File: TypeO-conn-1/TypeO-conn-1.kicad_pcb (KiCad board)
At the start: 2 copper layers, 5 parts, among them J1 USB_C_Receptacle_USB2.0, J2 , SW1 SW_DIP_x01

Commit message: Update PCB
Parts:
- moved J2 2.54 mm to (124.5, 76.2)
- moved SW1 2.54 mm to (119.4, 86.4)
- moved R2 1.79 mm to (112.5, 76.2)
- moved R1 1.46 mm to (114.3, 83.6)
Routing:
- net Net-(J1-PadA6): track 23.7 -> 16.0 mm, vias 0 -> 1
- net Net-(J1-PadA1): track 31.5 -> 24.7 mm
- net Net-(J1-PadA4): track 19.3 -> 16.9 mm
- net Net-(SW1-Pad2): track 7.88 -> 5.64 mm
- net Net-(J1-PadA5): track 13.6 -> 11.8 mm
- net Net-(J1-PadA7): track 18.6 -> 16.8 mm
- net Net-(J1-PadB5): track 14.1 -> 13.3 mm
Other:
- board outline added: 24 x 19.6 mm
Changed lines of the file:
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@@
     (property "Sheetname" "")
     (attr smd)
-    (fp_text reference "J1" (at -6.670499 0.12134 180) (layer "F.SilkS")
+    (fp_text reference "J1" (at -6.404035 -0.274964 180) (layer "F.SilkS")
       (effects (font (size 1 1) (thickness 0.15)))
     )
@@
   )
   (footprint "Resistor_THT:R_Axial_DIN0207_L6.3mm_D2.5mm_P7.62mm_Horizontal" (layer "F.Cu")
-    (at 114.3 76.2)
+    (at 112.505976 76.246718)
     (descr "Resistor, Axial_DIN0207 series, Axial, Horizontal, pin pitch=7.62mm, 0.25W = 1/4W, length*diameter=6.3*2.5mm^2, http://cdn-reichelt.de/documents/datenblatt/B400/1_4W%23YAG.pdf")
     (tags "Resistor Axial_DIN0207 series Axial Horizontal pin pitch 7.62mm 0.25W = 1/4W length 6.3mm diameter 2.5mm")
@@
     (property "Sheetname" "")
     (attr through_hole)
-    (fp_text reference "R2" (at 1.522976 -2.602604) (layer "F.SilkS")
-      (effects (font (size 1 1) (thickness 0.15)))
-    )
-    (fp_text value "10K" (at 5.08 -2.54) (layer "F.Fab")
+    (fp_text reference "R2" (at 1.848743 2.473275) (layer "F.SilkS")
+      (effects (font (size 1 1) (thickness 0.15)))
+    )
+    (fp_text value "10K" (at 5.54862 2.617426) (layer "F.Fab")
       (effects (font (size 1 1) (thickness 0.15)))
     )
@@
   )
   (footprint "Connector_PinHeader_2.54mm:PinHeader_1x05_P2.54mm_Vertical" (layer "F.Cu")
-    (at 127 76.2)
+    (at 124.46 76.2)
     (descr "Through hole straight pin header, 1x05, 2.54mm pitch, single row")
     (tags "Through hole pin header THT 1x05 2.54mm single row")
@@
     (property "Sheetname" "")
     (attr through_hole)
-    (fp_text reference "J2" (at 0 -2.33) (layer "F.SilkS")
+    (fp_text reference "J2" (at -2.561376 2.231691) (layer "F.SilkS")
       (effects (font (size 1 1) (thickness 0.15)))
     )
@@
   )
   (footprint "Resistor_THT:R_Axial_DIN0207_L6.3mm_D2.5mm_P7.62mm_Horizontal" (layer "F.Cu")
-    (at 114.3 85.09 -90)
+    (at 114.327258 83.628569 -90)
     (descr "Resistor, Axial_DIN0207 series, Axial, Horizontal, pin pitch=7.62mm, 0.25W = 1/4W, length*diameter=6.3*2.5mm^2, http://cdn-reichelt.de/documents/datenblatt/B400/1_4W%23YAG.pdf")
     (tags "Resistor Axial_DIN0207 series Axial Horizontal pin pitch 7.62mm 0.25W = 1/4W length 6.3mm diameter 2.5mm")
@@
     (property "Sheetname" "")
     (attr through_hole)
-    (fp_text reference "R1" (at 1.4988 2.373258 180) (layer "F.SilkS")
-      (effects (font (size 1 1) (thickness 0.15)))
-    )
-    (fp_text value "10K" (at 4.719649 2.429764 90) (layer "F.Fab")
+    (fp_text reference "R1" (at 5.470301 2.951661 180) (layer "F.SilkS")
+      (effects (font (size 1 1) (thickness 0.15)))
+    )
+    (fp_text value "10K" (at 1.482121 2.375057 90) (layer "F.Fab")
       (effects (font (size 1 1) (thickness 0.15)))
     )
@@
   )
   (footprint "Button_Switch_SMD:SW_DIP_SPSTx01_Slide_Omron_A6S-110x_W8.9mm_P2.54mm" (layer "F.Cu")
-    (at 119.38 88.9 90)
+    (at 119.38 86.36 90)
     (descr "SMD 1x-dip-switch SPST Omron_A6S-110x, Slide, row spacing 8.9 mm (350 mils), body size  (see http://omronfs.omron.com/en_US/ecb/products/pdf/en-a6s.pdf)")
     (tags "SMD DIP Switch SPST Slide 8.9mm 350mil")
@@
     (property "Sheetname" "")
     (attr smd)
-    (fp_text reference "SW1" (at 1.802645 3.847967 180) (layer "F.SilkS")
+    (fp_text reference "SW1" (at -2.883021 3.75 180) (layer "F.SilkS")
       (effects (font (size 1 1) (thickness 0.15)))
     )
@@
     )
   )
-  (segment (start 114.3 88.9) (end 114.3 85.09) (width 0.25) (layer "F.Cu") (net 1))
-  (segment (start 127 86.36) (end 120.01 93.35) (width 0.25) (layer "F.Cu") (net 1))
-  (segment (start 113.59 84.38) (end 109.73 84.38) (width 0.25) (layer "F.Cu") (net 1))
-  (segment (start 114.3 85.09) (end 113.59 84.38) (width 0.25) (layer "F.Cu") (net 1))
-  (segment (start 114.3 76.2) (end 112.32 78.18) (width 0.25) (layer "F.Cu") (net 1))
-  (segment (start 118.75 93.35) (end 114.3 88.9) (width 0.25) (layer "F.Cu") (net 1))
-  (segment (start 112.32 78.18) (end 109.73 78.18) (width 0.25) (layer "F.Cu") (net 1))
-  (segment (start 119.38 93.35) (end 118.75 93.35) (width 0.25) (layer "F.Cu") (net 1))
-  (segment (start 120.01 93.35) (end 119.38 93.35) (width 0.25) (layer "F.Cu") (net 1))
-  (segment (start 121.454211 75.075489) (end 117.5997 78.93) (width 0.25) (layer "F.Cu") (net 2))
-  (segment (start 117.5997 78.93) (end 109.73 78.93) (width 0.25) (layer "F.Cu") (net 2))
-  (segment (start 127 76.2) (end 125.875489 75.075489) (width 0.25) (layer "F.Cu") (net 2))
-  (segment (start 125.875489 75.075489) (end 121.454211 75.075489) (width 0.25) (layer "F.Cu") (net 2))
-  (segment (start 121.92 76.2) (end 118.59 79.53) (width 0.25) (layer "F.Cu") (net 3))
-  (segment (start 118.59 79.53) (end 109.73 79.53) (width 0.25) (layer "F.Cu") (net 3))
+  (gr_line (start 127 73.66) (end 127 88.9) (layer "Edge.Cuts") (width 0.1))
+  (gr_line (start 127 88.9) (end 121.32202 93.135099) (layer "Edge.Cuts") (width 0.1))
+  (gr_line (start 112.288553 93.087049) (end 107.195216 88.089812) (layer "Edge.Cuts") (width 0.1))
+  (gr_line (start 103.062885 88.089812) (end 103.014836 73.578605) (layer "Edge.Cuts") (width 0.1))
+  (gr_line (start 107.195216 88.089812) (end 103.062885 88.089812) (layer "Edge.Cuts") (width 0.1))
+  (gr_line (start 121.32202 93.135099) (end 112.288553 93.087049) (layer "Edge.Cuts") (width 0.1))
+  (gr_line (start 103.014836 73.578605) (end 106.68 73.578605) (layer "Edge.Cuts") (width 0.1))
+  (gr_line (start 106.68 73.578605) (end 127 73.66) (layer "Edge.Cuts") (width 0.1))
+  (segment (start 114.327258 85.757258) (end 119.38 90.81) (width 0.5) (layer "F.Cu") (net 1))
+  (segment (start 113.575827 84.38) (end 114.327258 83.628569) (width 0.5) (layer "F.Cu") (net 1))
+  (segment (start 120.01 90.81) (end 124.46 86.36) (width 0.5) (layer "F.Cu") (net 1))
+  (segment (start 119.38 90.81) (end 120.01 90.81) (width 0.5) (layer "F.Cu") (net 1))
+  (segment (start 110.572694 78.18) (end 109.73 78.18) (width 0.5) (layer "F.Cu") (net 1))
+  (segment (start 114.327258 83.628569) (end 114.327258 85.757258) (width 0.5) (layer "F.Cu") (net 1))
+  (segment (start 109.73 84.38) (end 113.575827 84.38) (width 0.5) (layer "F.Cu") (net 1))
+  (segment (start 112.505976 76.246718) (end 110.572694 78.18) (width 0.5) (layer "F.Cu") (net 1))
+  (segment (start 116.918282 74.997207) (end 112.985489 78.93) (width 0.5) (layer "F.Cu") (net 2))
+  (segment (start 112.985489 78.93) (end 109.73 78.93) (width 0.5) (layer "F.Cu") (net 2))
+  (segment (start 123.257207 74.997207) (end 116.84 74.997207) (width 0.5) (layer "F.Cu") (net 2))
+  (segment (start 124.46 76.2) (end 123.257207 74.997207) (width 0.5) (layer "F.Cu") (net 2))
+  (segment (start 116.842694 79.53) (end 109.73 79.53) (width 0.25) (layer "F.Cu") (net 3))
+  (segment (start 120.125976 76.246718) (end 116.842694 79.53) (width 0.25) (layer "F.Cu") (net 3))
+  (segment (start 114.327258 91.248569) (end 113.12539 91.248569) (width 0.25) (layer "F.Cu") (net 5))
   (segment (start 107.88048 83.595498) (end 108.945978 82.53) (width 0.25) (layer "F.Cu") (net 5))
-  (segment (start 107.88048 86.29048) (end 107.88048 83.595498) (width 0.25) (layer "F.Cu") (net 5))
   (segment (start 108.945978 82.53) (end 109.73 82.53) (width 0.25) (layer "F.Cu") (net 5))
-  (segment (start 114.3 92.71) (end 107.88048 86.29048) (width 0.25) (layer "F.Cu") (net 5))
-  (segment (start 121.190229 77.565489) (end 127.486499 77.565489) (width 0.25) (layer "F.Cu") (net 10))
-  (segment (start 109.73 81.03) (end 117.725718 81.03) (width 0.25) (layer "F.Cu") (net 10))
-  (segment (start 128.174511 80.105489) (end 127 81.28) (width 0.25) (layer "F.Cu") (net 10))
-  (segment (start 117.725718 81.03) (end 121.190229 77.565489) (width 0.25) (layer "F.Cu") (net 10))
-  (segment (start 128.174511 78.253501) (end 128.174511 80.105489) (width 0.25) (layer "F.Cu") (net 10))
-  (segment (start 127.486499 77.565489) (end 128.174511 78.253501) (width 0.25) (layer "F.Cu") (net 10))
-  (segment (start 109.73 82.03) (end 123.71 82.03) (width 0.25) (layer "F.Cu") (net 11))
-  (segment (start 123.71 82.03) (end 127 78.74) (width 0.25) (layer "F.Cu") (net 11))
-  (segment (start 126.37 84.45) (end 127 83.82) (width 0.25) (layer "F.Cu") (net 12))
-  (segment (start 119.38 84.45) (end 126.37 84.45) (width 0.25) (layer "F.Cu") (net 12))
+  (segment (start 113.12539 91.248569) (end 107.88048 86.003659) (width 0.25) (layer "F.Cu") (net 5))
+  (segment (start 107.88048 86.003659) (end 107.88048 83.595498) (width 0.25) (layer "F.Cu") (net 5))
+  (segment (start 117.931641 79.597769) (end 120.273755 79.597769) (width 0.25) (layer "F.Cu") (net 10))
+  (segment (start 109.73 81.03) (end 116.49941 81.03) (width 0.25) (layer "F.Cu") (net 10))
+  (segment (start 116.49941 81.03) (end 117.931641 79.597769) (width 0.25) (layer "F.Cu") (net 10))
+  (via (at 120.273755 79.597769) (size 0.8) (drill 0.4) (layers "F.Cu" "B.Cu") (net 10))
+  (segment (start 121.955986 81.28) (end 120.273755 79.597769) (width 0.25) (layer "B.Cu") (net 10))
+  (segment (start 124.46 81.28) (end 121.955986 81.28) (width 0.25) (layer "B.Cu") (net 10))
+  (segment (start 123.71 78.74) (end 124.46 78.74) (width 0.25) (layer "F.Cu") (net 11))
+  (segment (start 118.269603 80.486115) (end 122.713885 80.486115) (width 0.25) (layer "F.Cu") (net 11))
+  (segment (start 116.725718 82.03) (end 118.269603 80.486115) (width 0.25) (layer "F.Cu") (net 11))
+  (segment (start 109.73 82.03) (end 116.725718 82.03) (width 0.25) (layer "F.Cu") (net 11))
+  (segment (start 122.713885 80.486115) (end 124.46 78.74) (width 0.25) (layer "F.Cu") (net 11))
+  (segment (start 119.38 82.47952) (end 119.94952 82.47952) (width 0.25) (layer "F.Cu") (net 12))
+  (segment (start 121.29 83.82) (end 124.46 83.82) (width 0.25) (layer "F.Cu") (net 12))
+  (segment (start 119.94952 82.47952) (end 121.29 83.82) (width 0.25) (layer "F.Cu") (net 12))
 )

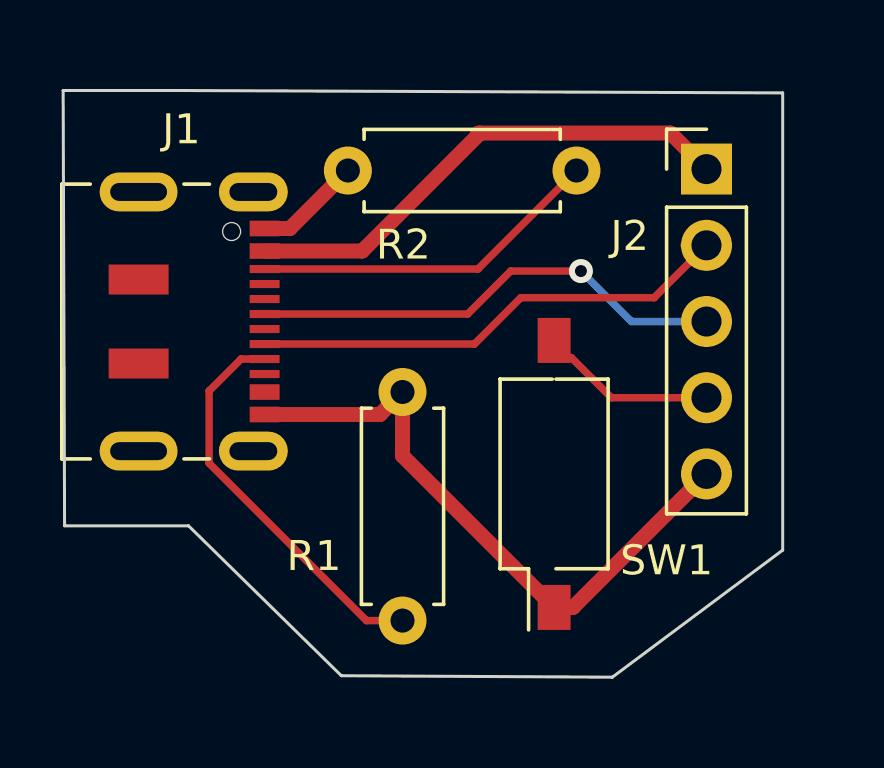
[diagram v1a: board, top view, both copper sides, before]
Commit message: Update PCB to add jumpers
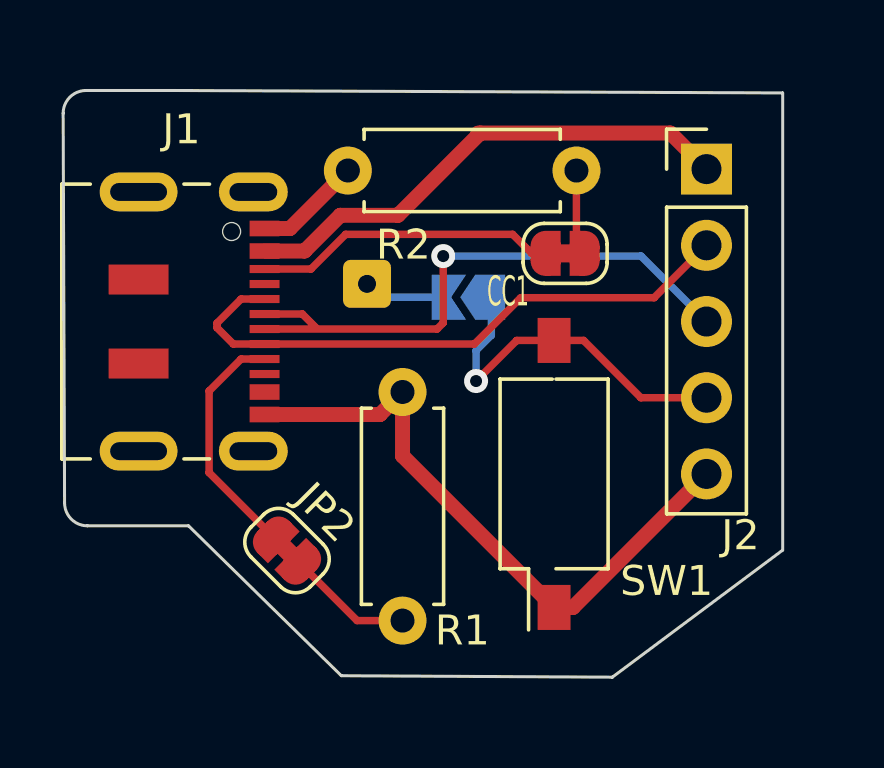
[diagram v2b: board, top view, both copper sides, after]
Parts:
- added H1: ID, Connector_Wire:SolderWire-0.1sqmm_1x01_D0.4mm_OD1mm, B.Cu at (113.1, 80.0)
- added JP1: SolderJumper_2_Open, Jumper:SolderJumper-2_P1.3mm_Open_TrianglePad1.0x1.5mm, B.Cu at (116.5, 80.5)
- added JP2: CC2, Jumper:SolderJumper-2_P1.3mm_Bridged_RoundedPad1.0x1.5mm, F.Cu at (110.5, 88.9)
- added JP3: CC1, Jumper:SolderJumper-2_P1.3mm_Bridged_RoundedPad1.0x1.5mm, F.Cu at (119.7, 79.0)
- J2: value (none) -> Conn_01x05_Male
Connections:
- J1 pad B6: unconnected-(J1-PadB6) -> Net-(J1-PadA6)
- J1 pad B7: unconnected-(J1-PadB7) -> Net-(J1-PadA7)
- R1 pad 2: Net-(J1-PadB5) -> Net-(R1-Pad2)
- R2 pad 2: Net-(J1-PadA5) -> Net-(R2-Pad2)
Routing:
- net Net-(J2-Pad4): track 5.64 -> 12.1 mm, vias 0 -> 1
- net Net-(J1-PadB5): track 13.3 -> 8.04 mm
- net Net-(R1-Pad2): track 0.00 -> 4.17 mm
- net Net-(J1-PadA6): track 16.0 -> 19.8 mm
- net Net-(J1-PadA7): track 16.8 -> 20.0 mm
- net Net-(R2-Pad2): track 0.00 -> 2.87 mm
- net Net-(H1-Pad1): track 0.00 -> 2.84 mm
- net Net-(J1-PadA5): track 11.8 -> 10.1 mm
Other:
- outline, holes or cut-outs redrawn
- board text added: "TypeO-conn proto-1"
